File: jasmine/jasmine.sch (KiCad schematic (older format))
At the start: 27 parts, among them J1 NEIGHBOR1, J2 NEIGHBOR2, J3 USB-MICRO-B-SHIELDED, J4 LIPO_BATT_CONN, J7 BONUS_ROW, P1 TEST_POINT, P2 TEST_POINT, P3 TEST_POINT, P5 3.7_VDC, U1 MCP73831T

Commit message: JASMINE: Revised charge rate config; Added DNP JST connector; Added DNP screw terminal; Added load switch w/ LED indicator; Updated labeling on silkscreen LUCKY BAMBOO: updated soldermask clearance
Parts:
- added D4: LED, gsg-modules:0603D, symbol jasmine-rescue:LED
- added J5: 2PIN_BATT_CONN, gsg-modules:JST_PH_S2B-PH-SM4-TB_02x2.00mm_Angled, symbol jasmine-rescue:2PIN_BATT_CONN
- added P4: 3.7_VDC, gsg-modules:TerminalBlock_4UCON_19963_02x3.5mm_Straight, symbol Connector:Screw_Terminal_01x02
- added R7: 330, gsg-modules:0603, symbol jasmine-rescue:R
- added R8: 0, gsg-modules:0603, symbol Device:R
- added SW1: SW_SPDT, gsg-modules:MHSS1105, symbol Switch:SW_SPDT
- C1, C2: symbol C -> jasmine-rescue:C
- D1, D2: symbol D -> jasmine-rescue:D
- D3: symbol LED -> jasmine-rescue:LED
- J1, J2: symbol CONN_02X20 -> jasmine-rescue:CONN_02X20
- J3: symbol USB-MICRO-B-SHIELDED -> jasmine-rescue:USB-MICRO-B-SHIELDED
- J4: footprint Connectors_JST:JST_PH_S2B-PH-SM4-TB_02x2.00mm_Angled -> gsg-modules:JST_PH_S2B-PH-SM4-TB_02x2.00mm_Angled; symbol 2PIN_BATT_CONN -> jasmine-rescue:2PIN_BATT_CONN
- J7: symbol CONN_01X20 -> jasmine-rescue:CONN_01X20
- MH1, MH2, MH3, MH4: symbol CONN_01X01 -> jasmine-rescue:CONN_01X01
- P1, P2, P3: symbol CONN_01X02 -> Connector_Generic:Conn_01x02; Note (none) -> DNP
- P5: symbol 2PIN_BATT_CONN -> jasmine-rescue:2PIN_BATT_CONN; Note (none) -> DNP
- R1, R4, R5, R6: symbol R -> jasmine-rescue:R
- R2: value 10k -> 7.5k; symbol R -> jasmine-rescue:R; Description RES SMD 10K OHM 1% 1/10W 0603 -> RES 7.5K OHM 1% 1/10W 0603; Manufacturer Yageo -> Stackpole; Part Number RC0603FR-0710KL -> RMCF0603FT7K50
- R3: symbol R -> jasmine-rescue:R; Note DNP -> (none)
- U1: symbol MCP73831T -> jasmine-rescue:MCP73831T
- W1, W2: symbol TEST_2P -> jasmine-rescue:TEST_2P
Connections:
- wire segments 167 -> 203
- no-connect marks 96 -> 97
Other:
- note added: "R2 and R3 are configured for a 100mA charge rate.\nTo reconfigure for a 500mA charge rate, remove the\n7.5 kOhm resistor from R2 and bridge the pads."
- note removed: "The 10k resistors on R2 configures the charge \ncurrent to be 100mA which is the fastest \nsupported charge rate for many LiPo batteries. \nThe charge rate can be reconfigured changing \nthe R2 resistor or adding a resistor to R3."

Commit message: Rev 2! Added 2 MUXs and an I/O expander for controlling charge rate, and reading current rates from your GreatFET. Also added a 32 MHz oscillator for eventual GreatFET sleep mode.
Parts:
- removed P3: TEST_POINT, gsg-modules:HEADER-1x2, symbol Connector_Generic:Conn_01x02
- removed R2: 7.5k, gsg-modules:0603, symbol jasmine-rescue:R
- removed R3: 2.5k, gsg-modules:0603, symbol jasmine-rescue:R
- removed R4: 100k, gsg-modules:0603, symbol jasmine-rescue:R
- added C?: C, gsg-modules:0603, symbol Device:C
- added D? (x3): LED, symbol Device:LED
- added P?: INPUT, gsg-modules:TerminalBlock_4UCON_19963_02x3.5mm_Straight, symbol Connector:Screw_Terminal_01x02
- added R?: 0.1, gsg-modules:0603, symbol Device:R
- added R? (x10): 10k, gsg-modules:0603, symbol jasmine-rescue:R
- added R? (x6): 10k, symbol Device:R
- added R? (x4): 0, gsg-modules:0603, symbol Device:R
- added R? (x3): 330, gsg-modules:0603, symbol jasmine-rescue:R
- added R? (x2): 67k, symbol Device:R
- added R?: 2k, symbol Device:R
- added R?: 2.5k, symbol Device:R
- added R?: 3.33k, symbol Device:R
- added R?: 5k, symbol Device:R
- added R?: 25k, symbol Device:R
- added R?: R, gsg-modules:RESISTOR-AXIAL-2.3x6.0mm, symbol Device:R
- added T? (x4): Jumper, symbol Connector:TestPoint_2Pole
- added TP? (x3): (no value), symbol Connector:TestPoint
- added U? (x2): 74HC4051, symbol narcissus-rescue:74HC4051
- added U?: PCA9674, symbol gsg-symbols:PCA9674
- added X?: SiT1533, gsg-modules:SiT1533, symbol gsg-symbols:SiT1533
- J7: Note DNP -> (none)
- R1: Description RES 330 OHM 1/10W 5% 0603 SMD -> RES 330 OHM 1/10W 1% 0603 SMD; Part Number RMCF0603JT330R -> RMCF0603FT330R
- R5: value 100k -> 10k; Description RES SMD 100K OHM 1% 1/10W 0603 -> RES 10K OHM 1% 1/8W 0603; Manufacturer Yageo -> Stackpole; Part Number RC0603FR-07100KL -> RNCP0603FTD10K0
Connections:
- net +5V: now also R?.2
- net GND: now also C?.2, D?.1 (K), D?.1 (K), D?.1 (K), R?.1, R?.1, R?.1, R?.2, R?.2, R?.2, TP?.1, TP?.1, U?.3 (Z), U?.7 (VEE), U?.7 (VEE), U?.8 (GND), U?.8 (GND), U?.8 (VSS), X?.2 (GND); no longer J7.10 (P10)
- net I2C0_SCL: now also U?.14 (SCL)
- net I2C0_SDA: now also U?.15 (SDA)
- net VBAT: now also J5.1 (P2), P4.2 (Pin_2), P5.2 (P1), R7.1, R8.1, SW1.1 (A)
- net 3.3V: now reaches J7.20 (P20)
- net 3.3V: now also X?.4 (VDD)
- net BATT: now reaches C2.2, J4.1 (P2), SW1.2 (B), U1.3 (VBAT)
- net BATT: now also R?.1
- net STAT: now reaches C1.2, R1.1, U1.4 (VIN)
- net STAT: now also R?.1, R?.1, R?.2; no longer D1.1 (K), J3.1 (VBUS), P1.1 (Pin_1)
- net PROG: now reaches U1.5 (PROG)
- net PROG: now also R?.2, R?.2, R?.2, R?.2, R?.2, R?.2, R?.2, R?.2, R?.2, R?.2
- net at R5.1, R6.1, W1.2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: now also U?.3 (Z)
- new net: R?.1, U?.1 (Y4) (x2)
- new net: R?.2, U?.12 (Y3)
- new net: R?.2, U?.13 (Y0)
- new net: R?.2, U?.14 (Y1)
- new net: R?.2, U?.15 (Y2)
- new net: R?.1, U?.2 (Y6) (x2)
- new net: R?.2, U?.4 (Y7)
- new net: R?.1, U?.5 (Y5) (x2)
- new net: R?.1, U?.12 (Y3)
- new net: R?.1, R?.1, U?.13 (Y0)
- new net: R?.1, U?.14 (Y1)
- new net: R?.1, U?.15 (Y2)
- new net: R?.1, U?.4 (Y7)
- new net: R?.2, U?.1 (AD0)
- new net: R?.1, U?.2 (AD1)
- new net: R?.1, U?.3 (AD2)
- new net: D?.2 (A), R?.2 (x3)
- new net: P?.1 (Pin_1), R?.2, T?.1
- new net: P?.2 (Pin_2), R?.1, T?.2, T?.2
- new net: R?.1, X?.3 (CLK_OUT)
- new net LOAD: R?.1
- new net MEASURE_E: U?.12 (P7), U?.6 (~E~)
- new net MEASURE_S0: U?.11 (P6), U?.11 (S0)
- new net MEASURE_S1: U?.10 (P5), U?.10 (S1)
- new net MEASURE_S2: U?.9 (P4), U?.9 (S2)
- new net PZ1: T?.1
- new net PZ2: T?.2
- new net RATE_E: R?.1, R?.1, U?.4 (P0), U?.6 (~E~)
- new net RATE_S0: R?.1, R?.2, U?.11 (S0), U?.5 (P1)
- new net RATE_S1: R?.1, R?.2, U?.10 (S1), U?.6 (P2)
- new net RATE_S2: R?.1, R?.1, U?.7 (P3), U?.9 (S2)
- new net RTCX1: C?.1, J7.10 (P10), R?.2
- new net VBUS: D1.1 (K), J3.1 (VBUS), P1.1 (Pin_1), R?.1, R?.1, R?.2, R?.2, R?.2, T?.2, TP?.1, U?.16 (VCC), U?.16 (VCC), U?.16 (VDD)
- new net VCC: R?.2
- new net VINa: T?.1
- new net VOUTa: T?.1
- no-connect marks 97 -> 95
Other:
- note added: "Add switch for E/ADC pin."
- note added: "Default charge rate is set to 15mAh.\nUse GreatFET to reconfigure charge rate,\nor populate R? to change default charge rate.\nFIXME Add specific values for R?."
- note added: "Need to include a pads to I2C\npins for re-addressing (?)"
- note removed: "R2 and R3 are configured for a 100mA charge rate.\nTo reconfigure for a 500mA charge rate, remove the\n7.5 kOhm resistor from R2 and bridge the pads."
- moved on the sheet: J5, P2, R5, R6, W1, W2

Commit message: Removed all 'rescue' symbols
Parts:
- C1, C2: symbol jasmine-rescue:C -> Device:C
- D1, D2: symbol jasmine-rescue:D -> Device:D
- D3, D4: symbol jasmine-rescue:LED -> Device:LED
- J1, J2: symbol jasmine-rescue:CONN_02X20 -> Connector_Generic:Conn_02x20_Odd_Even
- J3: symbol jasmine-rescue:USB-MICRO-B-SHIELDED -> gsg-symbols:USB-MICRO-B-SHIELDED
- J4, J5, P5: symbol jasmine-rescue:2PIN_BATT_CONN -> Connector_Generic:Conn_01x02
- J7: symbol jasmine-rescue:CONN_01X20 -> Connector_Generic:Conn_01x20
- MH1, MH2, MH3, MH4: symbol jasmine-rescue:CONN_01X01 -> Connector_Generic:Conn_01x01
- R1, R5, R6, R7, R? (x13): symbol jasmine-rescue:R -> Device:R
- U1: symbol jasmine-rescue:MCP73831T -> gsg-symbols:MCP73831T
- U? (x2): symbol narcissus-rescue:74HC4051 -> gsg-symbols:74HC4051
- W1, W2: symbol jasmine-rescue:TEST_2P -> Connector:TestPoint_2Pole
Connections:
- net BATT: now also J4.2 (Pin_2); no longer J4.1 (P2)
- net GND: now also J4.1 (Pin_1), J5.1 (Pin_1), P5.2 (Pin_2); no longer J4.2 (P1), J5.2 (P1), P5.1 (P2)
- net VBAT: now also J5.2 (Pin_2), P5.1 (Pin_1); no longer J5.1 (P2), P5.2 (P1)

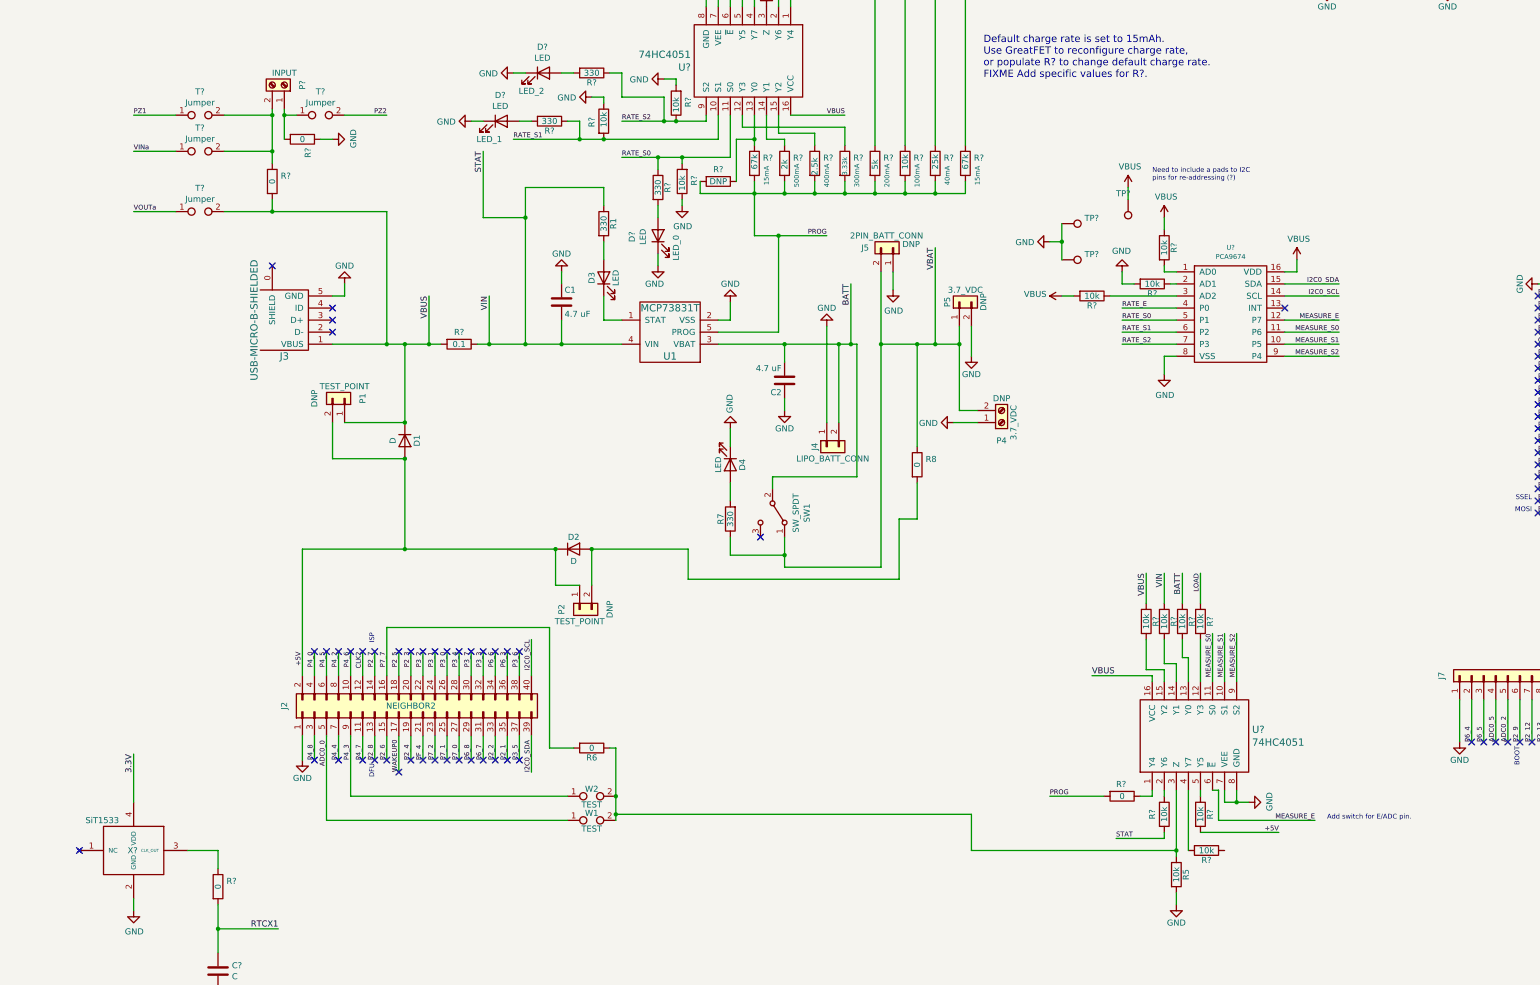
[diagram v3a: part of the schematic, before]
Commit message: Changed resistor on voltage divider MUX to 100k resistors; Added an optional voltage divider to screw terminal input
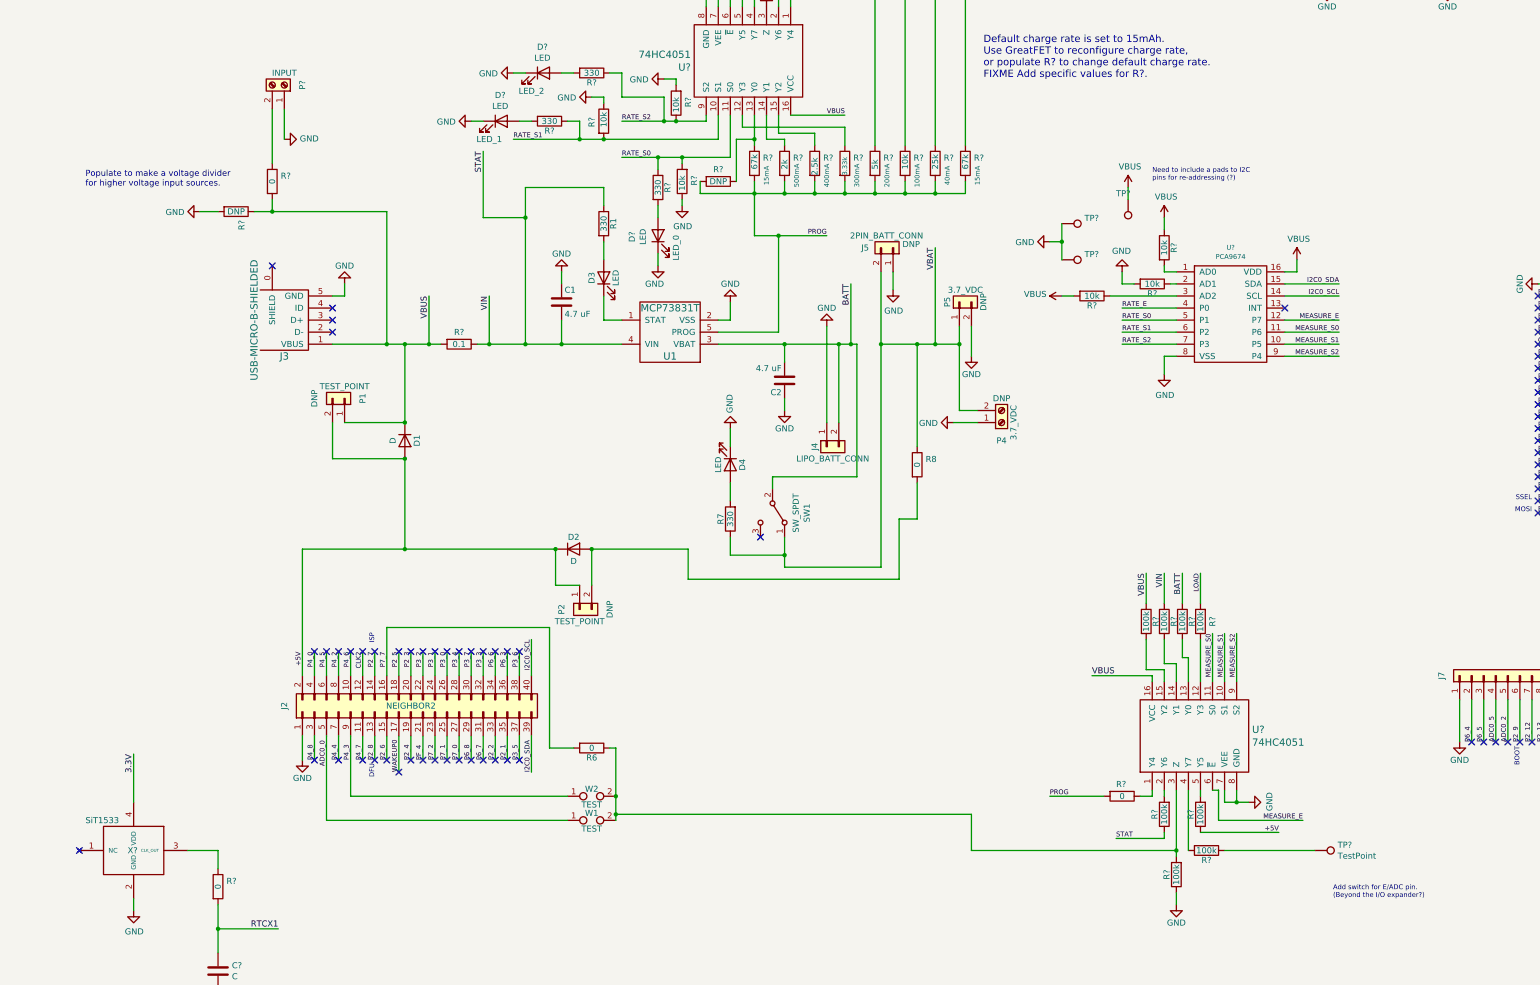
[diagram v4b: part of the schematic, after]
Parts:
- removed R5, R? (x6): 10k, gsg-modules:0603, symbol Device:R
- removed R?: 0, gsg-modules:0603, symbol Device:R
- removed T? (x4): Jumper, symbol Connector:TestPoint_2Pole
- added R? (x7): 100k, gsg-modules:0603, symbol Device:R
- added R?: DNP, gsg-modules:0603, symbol Device:R
- added TP?: TestPoint, symbol Connector:TestPoint
- R?: value 10k -> 100k; Description RES 10K OHM 1% 1/8W 0603 -> RES 100K OHM 1% 1/10W 0603; Part Number RNCP0603FTD10K0 -> RMCF0603FG100K
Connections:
- net +5V: now also R?.1
- net BATT: now also R?.1
- net GND: now also P?.1 (Pin_1), R?.1, R?.2
- net LOAD: now also R?.2
- net STAT: now also R?.1, R?.1
- net VBUS: now also R?.1, R?.1
- net at R6.1, U?.3 (Z), W1.2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: now also R?.2
- net at U?.12 (Y3): now also R?.1
- net at U?.13 (Y0): now also R?.2
- net at U?.14 (Y1): now also R?.2
- net at U?.15 (Y2): now also R?.2
- net at U?.2 (Y6): now also R?.2
- net at U?.5 (Y5): now also R?.2
- net at R?.1: now also TP?.1
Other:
- note added: "Add switch for E/ADC pin.\n(Beyond the I/O expander?)"
- note added: "Populate to make a voltage divider\nfor higher voltage input sources."
- note removed: "Add switch for E/ADC pin."

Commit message: Completed component and footprint selection
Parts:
- removed D? (x2): LED, symbol Device:LED
- removed R? (x6): 10k, symbol Device:R
- removed R?: 67k, symbol Device:R
- added D? (x2): LED, gsg-modules:0603D, symbol Device:LED
- added R?: 67k, gsg-modules:0603, symbol Device:R
- added R? (x6): 10k, gsg-modules:0603, symbol Device:R
- D?: footprint (none) -> gsg-modules:0603D; Description (none) -> LED YELLOW DIFFUSED 0603 SMD; Manufacturer (none) -> Rohm Semiconductor; Part Number (none) -> SML-D12Y8WT86
- R?: footprint (none) -> gsg-modules:0603; Description (none) -> RES 66.5K OHM 1% 1/10W 0603; Manufacturer (none) -> Stackpole; Part Number (none) -> RMCF0603FT66K5
- R?: footprint (none) -> gsg-modules:0603; Description (none) -> RES 2K OHM 1% 1/10W 0603; Manufacturer (none) -> Stackpole; Part Number (none) -> RMCF0603FT2K00
- R?: footprint (none) -> gsg-modules:0603; Description (none) -> RES 2.49K OHM 1% 1/10W 0603; Manufacturer (none) -> Stackpole; Part Number (none) -> RMCF0603FT2K49
- R?: footprint (none) -> gsg-modules:0603; Description (none) -> RES 3.32K OHM 1% 1/10W 0603; Manufacturer (none) -> Stackpole; Part Number (none) -> RMCF0603FG3K32
- R?: footprint (none) -> gsg-modules:0603; Description (none) -> RES 4.99K OHM 1% 1/10W 0603; Manufacturer (none) -> Stackpole; Part Number (none) -> RMCF0603FT4K99
- R?: footprint (none) -> gsg-modules:0603; Description (none) -> RES 24.9K OHM 1% 1/10W 0603; Manufacturer (none) -> Stackpole; Part Number (none) -> RMCF0603FT24K9
- U? (x2): footprint (none) -> gsg-modules:SOIC16; Description (none) -> IC MUX/DEMUX 8X1 16SOIC; Manufacturer (none) -> NXP; Part Number (none) -> 74HC4051D,653
- U?: footprint (none) -> gsg-modules:TSSOP16; Description (none) -> IC I/O EXPANDER I2C 8B 16TSSOP; Manufacturer (none) -> NXP; Part Number (none) -> PCA9674PW,118
- X?: Description (none) -> MEMS OSC XO 32.7680KHZ NANODRIVE; Manufacturer (none) -> SiTIME
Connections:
- net GND: now also D?.1 (K), D?.1 (K), R?.1, R?.1, R?.2, R?.2
- net PROG: now also R?.2, R?.2
- net RATE_E: now also R?.1, R?.1
- net RATE_S0: now also R?.1
- net RATE_S1: now also R?.2
- net RATE_S2: now also R?.2
- net VCC: now also R?.2
- net at U?.4 (Y7): now also R?.1
- net at U?.5 (Y5): now also R?.1
- net at R?.2: now also D?.2 (A) (x2)
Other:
- note added: "Test point is an open voltage divider.\nConnect to a current that you would\nlike to measure."

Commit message: Cleaned up jasmine.sch; Started Jasmine layout
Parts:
- TP1, TP2, TP3: renamed from TP?; footprint (none) -> gsg-modules:1Pin_0603
- TP4: renamed from TP?; footprint (none) -> gsg-modules:TESTPOINT-50MIL
- gave numbers to parts that had none: 42
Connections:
- net 3.3V is gone; now on net VCC: J7.20 (Pin_20), X1.4 (VDD)
- net LOAD is gone; now on net BATT_i: R35.2
- net VBUS: no longer D1.1 (K), J3.1 (VBUS), P1.1 (Pin_1), R28.1, R3.1, R4.2, R5.2
- net VCC: now also J1.2 (Pin_2)
- net BATT renamed BATT_i
- net PROG renamed PROG_i
- net STAT renamed STAT_i
- new net VBUS_i: D1.1 (K), J3.1 (VBUS), P1.1 (Pin_1), R28.1, R3.1, R4.2, R5.2
- no-connect marks 95 -> 93
